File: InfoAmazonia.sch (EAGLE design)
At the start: 83 parts, among them IC1 ADAFRUIT FONA, IC10 TL032C, IC11 NE555, IC12 CA3140AM Z, IC13 TL081BCDG4, IC2 LM2662, IC3 74HC4051, IC4 MIC29302AWD, IC5 4050D, IC6 4053D, IC7 4053D, IC8 4053D, IC9 SHT20, J1 BNCPTH, J2 BNCPTH, J3 BNCPTH, U1 ARDUINO-MEGAPRO, U2 MPL3115A2, U3 USD-SOCKETNEW, U4 ALS-PT19

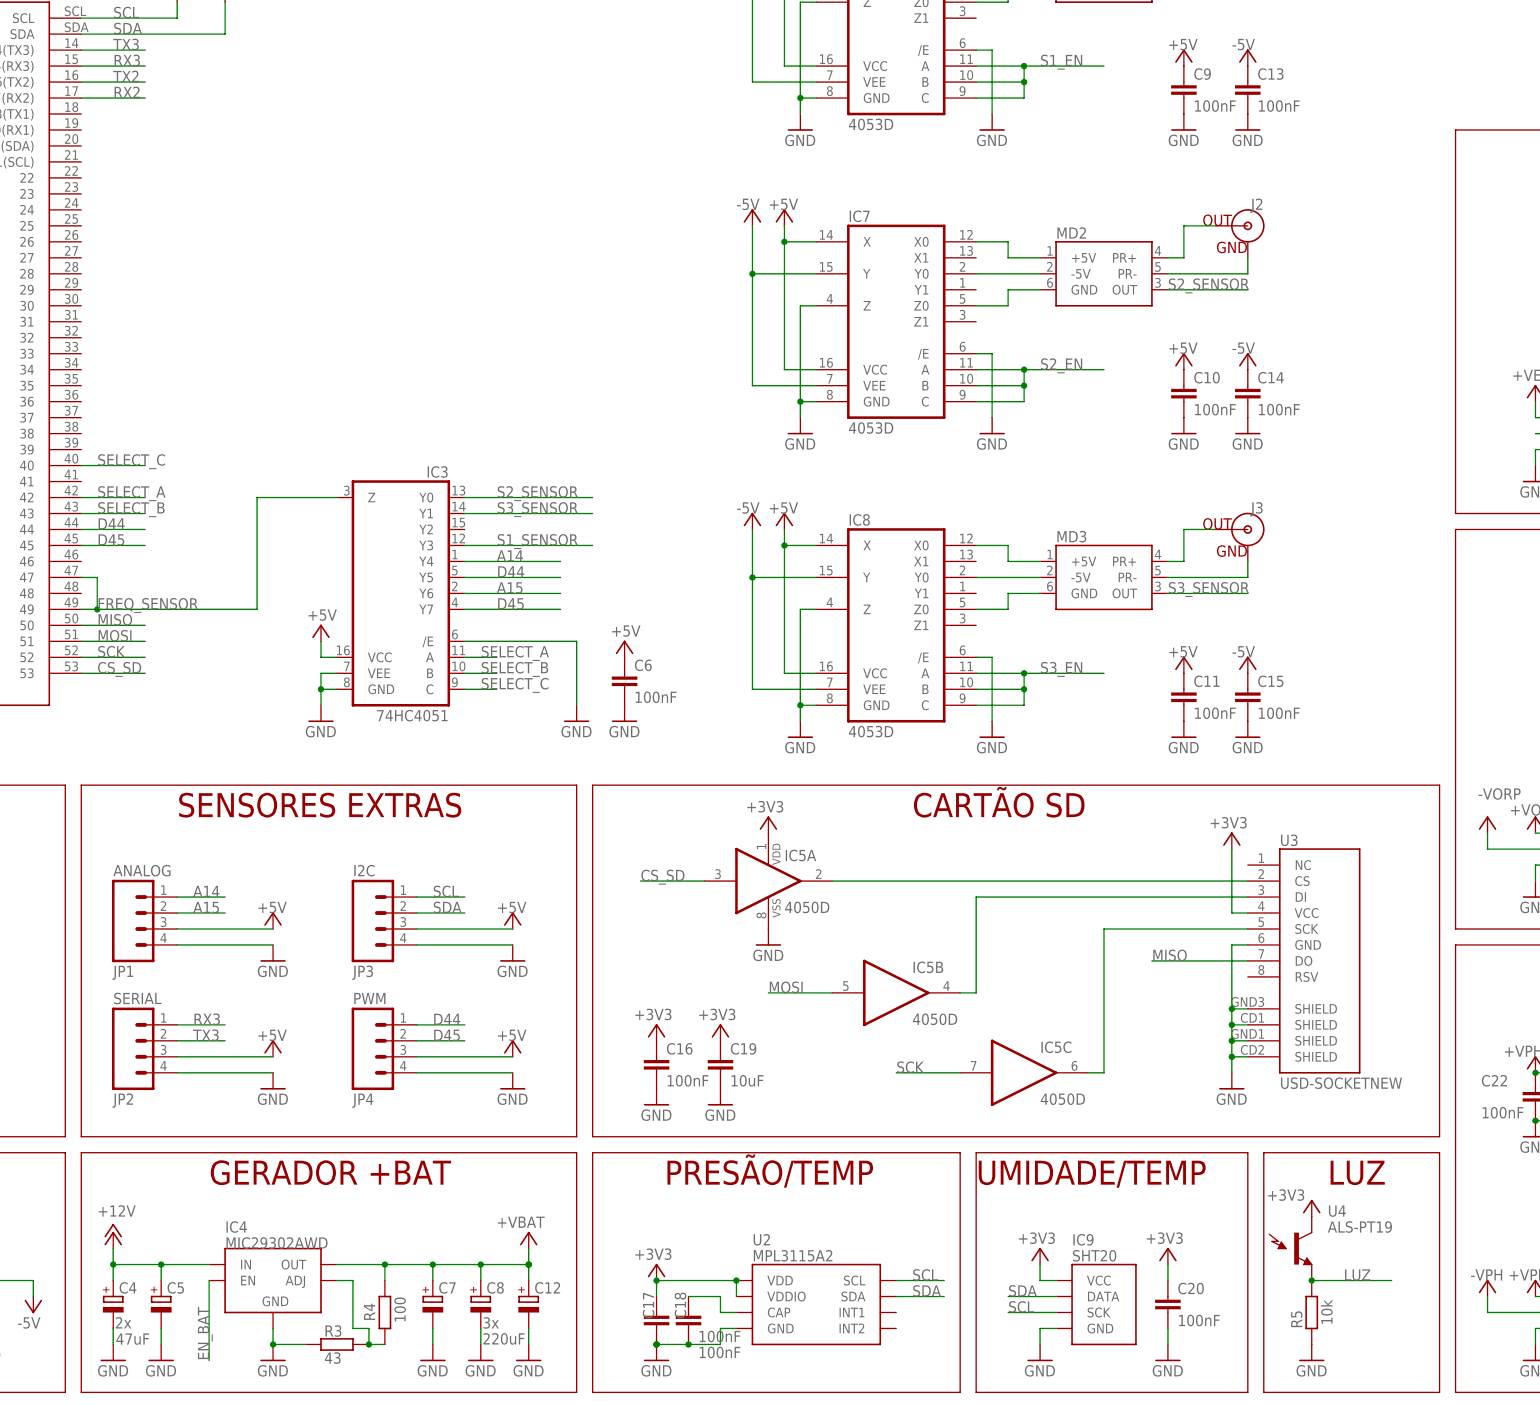
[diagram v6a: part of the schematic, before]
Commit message: - Mudado o codigo de alguns componentes para bater com o BOM
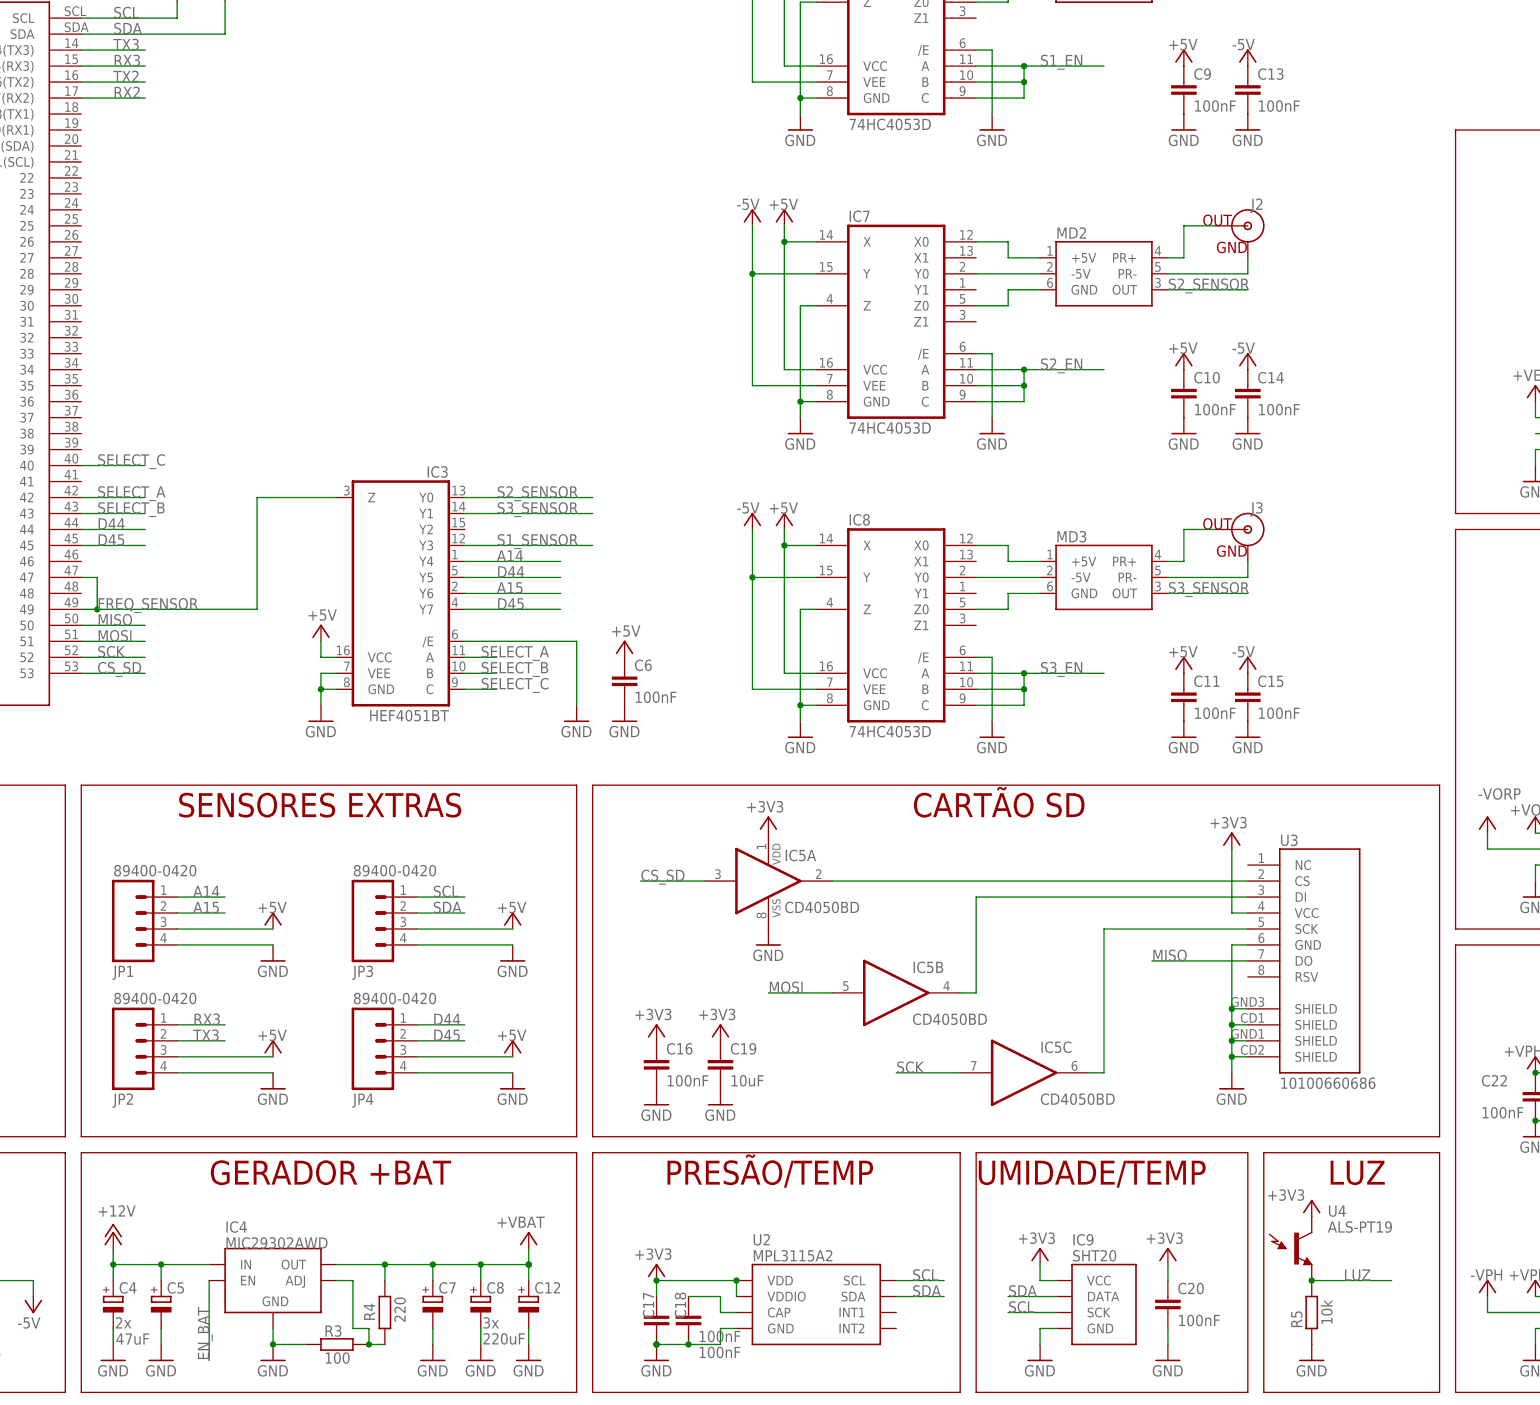
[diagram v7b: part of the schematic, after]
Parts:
- IC3: value 74HC4051 -> HEF4051BT
- IC5: value 4050D -> CD4050BD
- IC6, IC7, IC8: value 4053D -> 74HC4053D
- J1, J2, J3: value BNCPTH -> 31-5431-10RFX
- JP1: value ANALOG -> 89400-0420
- JP2: value SERIAL -> 89400-0420
- JP3: value I2C -> 89400-0420
- JP4: value PWM -> 89400-0420
- R3: value 43 -> 100
- R4: value 100 -> 220
- U3: value USD-SOCKETNEW -> 10100660686
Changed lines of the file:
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@@
 <part name="R9" library="InfoAmazonia" deviceset="R-EU_" device="R0603" value="75k"/>
 <part name="GND46" library="InfoAmazonia" deviceset="GND" device=""/>
-<part name="J1" library="InfoAmazonia" deviceset="BNC" device="PTH"/>
+<part name="J1" library="InfoAmazonia" deviceset="BNC" device="PTH" value="31-5431-10RFX"/>
 <part name="IC10" library="InfoAmazonia" deviceset="AMPOP_2" device="R" value="TL032C"/>
 <part name="GND51" library="InfoAmazonia" deviceset="GND" device=""/>
@@
 <part name="GND8" library="InfoAmazonia" deviceset="GND" device=""/>
 <part name="+VBAT2" library="InfoAmazonia" deviceset="+VBAT" device=""/>
-<part name="R4" library="InfoAmazonia" deviceset="R-EU_" device="R0603" value="100"/>
-<part name="R3" library="InfoAmazonia" deviceset="R-EU_" device="R0603" value="43"/>
+<part name="R4" library="InfoAmazonia" deviceset="R-EU_" device="R0603" value="220"/>
+<part name="R3" library="InfoAmazonia" deviceset="R-EU_" device="R0603" value="100"/>
 <part name="GND15" library="InfoAmazonia" deviceset="GND" device=""/>
 <part name="C5" library="InfoAmazonia" deviceset="CPOL-EU" device="UD6,3-5,8" value="47uF"/>
@@
 <part name="C2" library="InfoAmazonia" deviceset="CPOL-EU" device="SMC_B" value="47uF"/>
 <part name="C3" library="InfoAmazonia" deviceset="CPOL-EU" device="SMC_B" value="47uF"/>
-<part name="U3" library="InfoAmazonia" deviceset="USD-SOCKET" device="NEW"/>
+<part name="U3" library="InfoAmazonia" deviceset="USD-SOCKET" device="NEW" value="10100660686"/>
 <part name="+3V38" library="InfoAmazonia" deviceset="+3V3" device=""/>
 <part name="GND38" library="InfoAmazonia" deviceset="GND" device=""/>
-<part name="IC5" library="InfoAmazonia" deviceset="4050" device="D"/>
+<part name="IC5" library="InfoAmazonia" deviceset="4050" device="D" value="CD4050BD"/>
 <part name="+3V35" library="InfoAmazonia" deviceset="+3V3" device=""/>
 <part name="GND32" library="InfoAmazonia" deviceset="GND" device=""/>
@@
 <part name="P+18" library="InfoAmazonia" deviceset="+5V" device=""/>
 <part name="P-5" library="InfoAmazonia" deviceset="-5V" device=""/>
-<part name="JP1" library="InfoAmazonia" deviceset="M04" device="JST-PTH-VERT" value="ANALOG"/>
+<part name="JP1" library="InfoAmazonia" deviceset="M04" device="JST-PTH-VERT" value="89400-0420"/>
 <part name="GND10" library="InfoAmazonia" deviceset="GND" device=""/>
 <part name="P+10" library="InfoAmazonia" deviceset="+5V" device=""/>
-<part name="JP3" library="InfoAmazonia" deviceset="M04" device="JST-PTH-VERT" value="I2C"/>
+<part name="JP3" library="InfoAmazonia" deviceset="M04" device="JST-PTH-VERT" value="89400-0420"/>
 <part name="GND20" library="InfoAmazonia" deviceset="GND" device=""/>
 <part name="P+16" library="InfoAmazonia" deviceset="+5V" device=""/>
-<part name="JP2" library="InfoAmazonia" deviceset="M04" device="JST-PTH-VERT" value="SERIAL"/>
+<part name="JP2" library="InfoAmazonia" deviceset="M04" device="JST-PTH-VERT" value="89400-0420"/>
 <part name="GND11" library="InfoAmazonia" deviceset="GND" device=""/>
 <part name="P+11" library="InfoAmazonia" deviceset="+5V" device=""/>
-<part name="JP4" library="InfoAmazonia" deviceset="M04" device="JST-PTH-VERT" value="PWM"/>
+<part name="JP4" library="InfoAmazonia" deviceset="M04" device="JST-PTH-VERT" value="89400-0420"/>
 <part name="GND21" library="InfoAmazonia" deviceset="GND" device=""/>
 <part name="P+17" library="InfoAmazonia" deviceset="+5V" device=""/>
@@
 <part name="P-16" library="InfoAmazonia" deviceset="-VPH" device=""/>
 <part name="MD1" library="InfoAmazonia" deviceset="INFO-AMAZONIA-MODULE" device="" value="INFO-AMAZONIA-MODULE"/>
-<part name="J2" library="InfoAmazonia" deviceset="BNC" device="PTH"/>
-<part name="J3" library="InfoAmazonia" deviceset="BNC" device="PTH"/>
-<part name="MD4" library="InfoAmazonia" deviceset="INFO-AMAZONIA-MODULE" device="" value=""/>
+<part name="J2" library="InfoAmazonia" deviceset="BNC" device="PTH" value="31-5431-10RFX"/>
+<part name="J3" library="InfoAmazonia" deviceset="BNC" device="PTH" value="31-5431-10RFX"/>
+<part name="MD4" library="InfoAmazonia" deviceset="INFO-AMAZONIA-MODULE" device="" value="INFO-AMAZONIA-MODULE"/>
 <part name="GND42" library="InfoAmazonia" deviceset="GND" device=""/>
 <part name="GND45" library="InfoAmazonia" deviceset="GND" device=""/>
-<part name="MD6" library="InfoAmazonia" deviceset="INFO-AMAZONIA-MODULE" device="" value=""/>
+<part name="MD6" library="InfoAmazonia" deviceset="INFO-AMAZONIA-MODULE" device="" value="INFO-AMAZONIA-MODULE"/>
 <part name="GND58" library="InfoAmazonia" deviceset="GND" device=""/>
 <part name="GND59" library="InfoAmazonia" deviceset="GND" device=""/>
@@
 <part name="GND53" library="InfoAmazonia" deviceset="GND" device=""/>
 <part name="MD5" library="InfoAmazonia" deviceset="INFO-AMAZONIA-MODULE" device=""/>
-<part name="IC3" library="InfoAmazonia" deviceset="4051" device="D" value="74HC4051"/>
+<part name="IC3" library="InfoAmazonia" deviceset="4051" device="D" value="HEF4051BT"/>
 <part name="GND7" library="InfoAmazonia" deviceset="GND" device=""/>
 <part name="P+8" library="InfoAmazonia" deviceset="+5V" device=""/>
@@
 <part name="P+5" library="InfoAmazonia" deviceset="+5V" device=""/>
 <part name="P+7" library="InfoAmazonia" deviceset="+5V" device=""/>
-<part name="IC6" library="InfoAmazonia" deviceset="4053" device="D"/>
+<part name="IC6" library="InfoAmazonia" deviceset="4053" device="D" value="74HC4053D"/>
 <part name="GND33" library="InfoAmazonia" deviceset="GND" device=""/>
 <part name="GND29" library="InfoAmazonia" deviceset="GND" device=""/>
@@
 <part name="P-6" library="InfoAmazonia" deviceset="-5V" device=""/>
 <part name="MD2" library="InfoAmazonia" deviceset="INFO-AMAZONIA-MODULE" device="" value="INFO-AMAZONIA-MODULE"/>
-<part name="IC7" library="InfoAmazonia" deviceset="4053" device="D"/>
+<part name="IC7" library="InfoAmazonia" deviceset="4053" device="D" value="74HC4053D"/>
 <part name="GND34" library="InfoAmazonia" deviceset="GND" device=""/>
 <part name="GND30" library="InfoAmazonia" deviceset="GND" device=""/>
@@
 <part name="P-7" library="InfoAmazonia" deviceset="-5V" device=""/>
 <part name="MD3" library="InfoAmazonia" deviceset="INFO-AMAZONIA-MODULE" device="" value="INFO-AMAZONIA-MODULE"/>
-<part name="IC8" library="InfoAmazonia" deviceset="4053" device="D"/>
+<part name="IC8" library="InfoAmazonia" deviceset="4053" device="D" value="74HC4053D"/>
 <part name="GND35" library="InfoAmazonia" deviceset="GND" device=""/>
 <part name="C15" library="InfoAmazonia" deviceset="C-EU" device="C0603" value="100nF"/>
@@
 <instance part="MD4" gate="G$1" x="279.4" y="-114.3" smashed="yes">
 <attribute name="NAME" x="276.86" y="-121.412" size="1.778" layer="95"/>
-<attribute name="VALUE" x="271.78" y="-121.92" size="1.778" layer="95"/>
 </instance>
 <instance part="GND42" gate="1" x="266.7" y="-121.92" smashed="yes">
@@
 <instance part="MD6" gate="G$1" x="279.4" y="-40.64" smashed="yes">
 <attribute name="NAME" x="276.86" y="-47.752" size="1.778" layer="95"/>
-<attribute name="VALUE" x="271.78" y="-48.26" size="1.778" layer="95"/>
 </instance>
 <instance part="GND58" gate="1" x="266.7" y="-48.26" smashed="yes">

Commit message: - Adicionado o assembly drawing
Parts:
- IC12: value CA3140AM Z -> CA3140AMZ
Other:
- moved on the sheet: C21, C24, C29, IC11, MD5
